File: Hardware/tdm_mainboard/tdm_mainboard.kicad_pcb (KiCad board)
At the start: 2 copper layers, 60 x 100 mm, 72 parts, among them IC1 W25Q128JVSIQ, J1 Headphone, J2 LineIn, J3 Conn_02x06_Top_Bottom, U1 AP7313, U2 PAM8302AASCR, U3 SGTL5000, U4 Teensy4, U5 TPS61090RSAR, U6 MOUNTINGHOLE2.5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

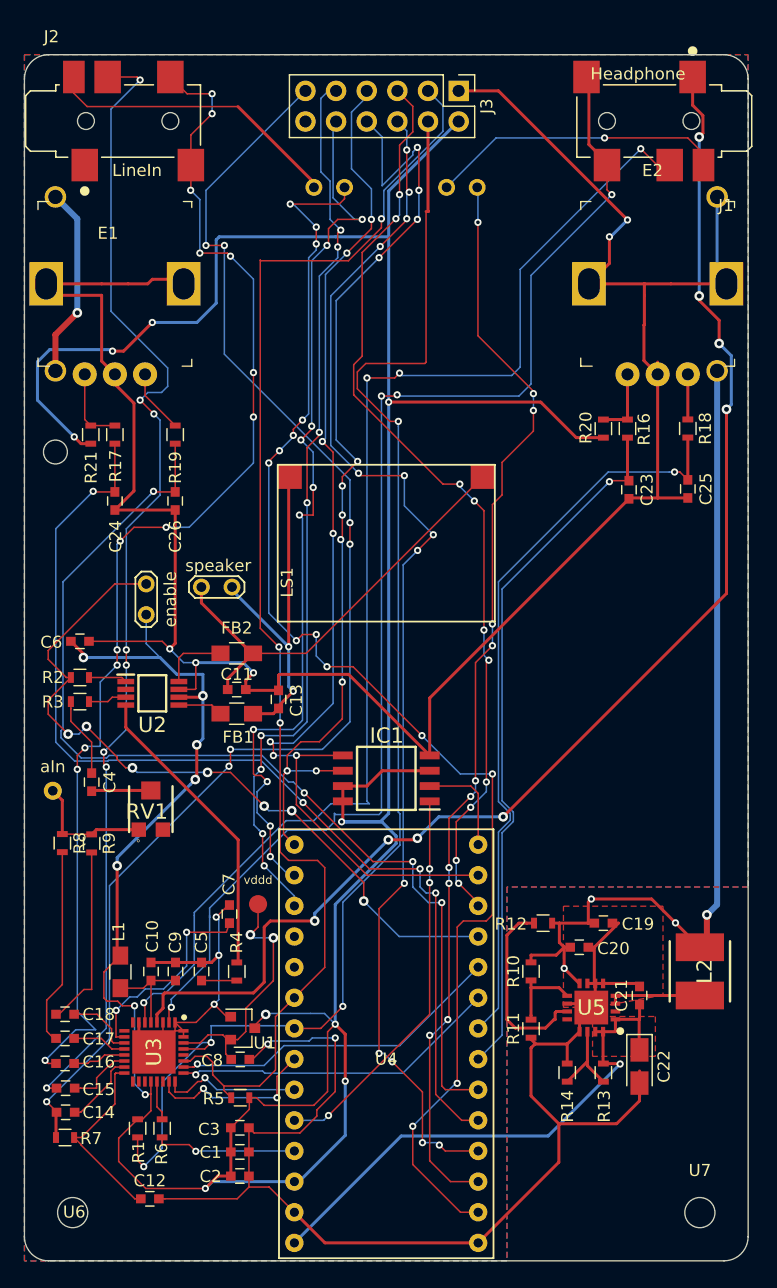
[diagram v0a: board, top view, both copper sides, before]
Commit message: some changes to the backboad
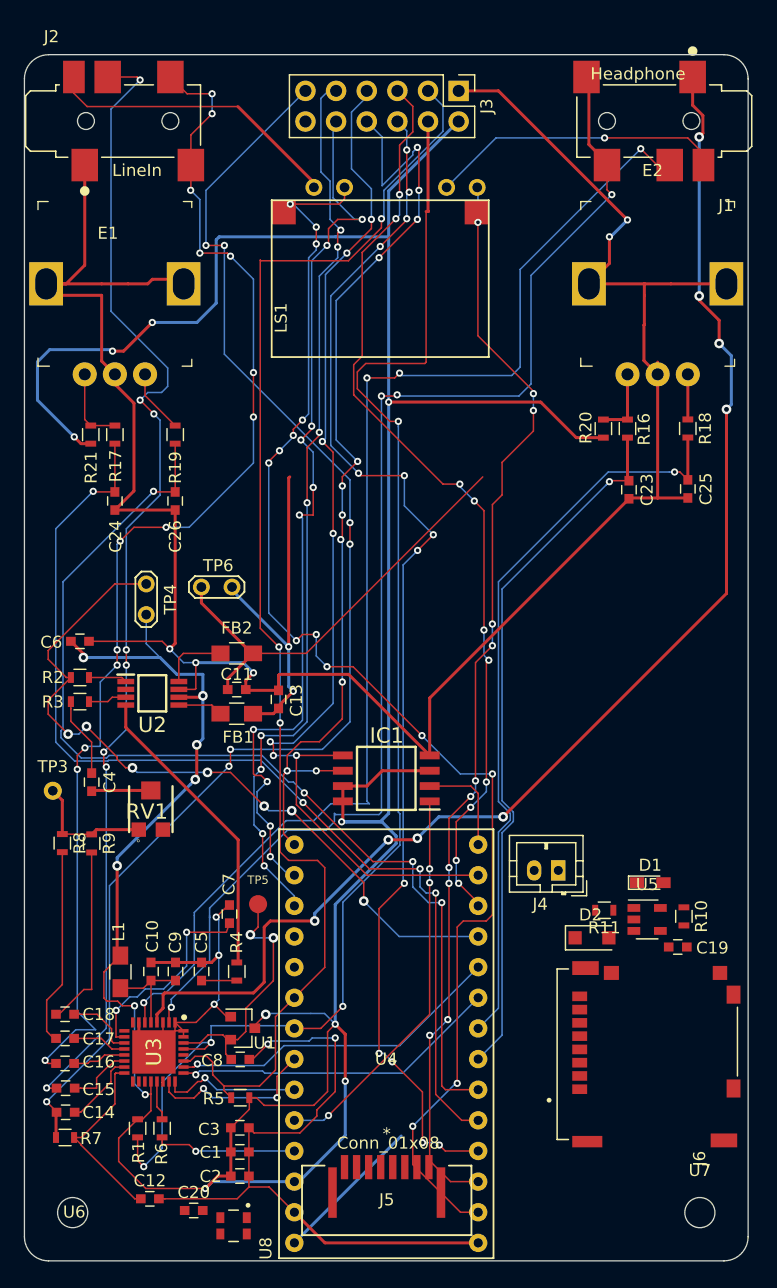
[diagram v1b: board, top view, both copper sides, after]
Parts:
- removed C21: 2.2uF, Capacitors_SMD:C_0603
- removed C22: 100uF electrolytic, Capacitors_Tantalum_SMD:CP_Tantalum_Case-A_EIA-3216-18_Reflow
- removed L2: VLC5045-6.8uH, SamacSys_Parts:INDPM5050X450N
- removed R12: 340K, Resistors_SMD:R_0603
- removed R13: 1.87M, Resistors_SMD:R_0603
- removed R14: 200K, Resistors_SMD:R_0603
- added D1: LED, LEDs:LED_0603_HandSoldering, F.Cu at (71.9, 88.6)
- added D2: mbr120, Diodes_SMD:D_SOD-123F, F.Cu at (67.1, 93.2)
- added J4: batteryConnection (jstph), Connectors_JST:JST_PH_B2B-PH-K_02x2.00mm_Straight, F.Cu at (64.3, 87.6)
- added J5: Conn_01x08, myLib:SFW8R-3STE1LF, F.Cu at (50.0, 109.5)
- added J6: 2908-05WB-MG, myLib:MOLEX_503182-1852_microsd, F.Cu at (72.4, 102.9)
- R10: value 1.87M -> 5k
- R11: value 340K -> 1k
- U5: value TPS61090RSAR -> MCP73831T-2ACI_OT; footprint SamacSys_Parts:QFN65P400X400X100-17N -> TO_SOT_Packages_SMD:SOT-23-5
- U8: value 1013 -> SPWmicrophone; footprint SamacSys_Parts:1013 -> myLib:MIC_SPW2430HR5H-B; moved to F.Cu
- moved U8 79.1 mm to (37.3, 117.1), turned to 270 degrees
- moved C20 38.7 mm to (34.0, 115.8)
- moved LS1 21.9 mm to (47.5, 36.1)
- moved R10 13.5 mm to (74.7, 91.4), turned to 270 degrees
- moved R11 11.5 mm to (68.1, 90.9), turned to 180 degrees
- moved U5 8.65 mm to (71.6, 91.7), turned to 0 degrees
- moved C19 6.48 mm to (74.2, 94.0)
- renumbered aIn to TP3, enable to TP4, vddd to TP5, speaker to TP6
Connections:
- C14 pad 2: MIC -> mic
- C20 pad 1: battery -> GND
- C20 pad 2: GND -> +3V3
- J3 pad 11: MIC -> (no net)
- R10 pad 2: battery -> GND
- R11 pad 1: GND -> Net-(R11-Pad1)
- R11 pad 2: Net-(R10-Pad1) -> Net-(D1-Pad1)
- R7 pad 1: MIC -> mic
- U3 pad 25: DIN -> DOUT
- U3 pad 26: DOUT -> DIN
- U4 pad Vin: 5.0V -> batteryPower
- U5 pad 1: 5.0V -> Net-(R11-Pad1)
- U5 pad 2: (no net) -> GND
- U5 pad 3: Net-(L2-PadP$2) -> battery
- U5 pad 4: Net-(L2-PadP$2) -> vbus
- U5 pad 5: GND -> Net-(R10-Pad1)
- U8 pad 1: Net-(U8-Pad1) -> GND
- U8 pad 2: Net-(U8-Pad1) -> +3V3
- U8 pad 3: GND -> mic
- U8 pad 4: battery -> (no net)
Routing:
- net battery: track 74.5 -> 0.00 mm, vias 4 -> 0
- net GND: track 340.0 -> 290.9 mm
- net 5.0V: track 45.5 -> 0.00 mm, vias 1 -> 0
- net Net-(U8-Pad1): track 15.9 -> 0.00 mm, vias 1 -> 0
- net /ENABLE: track 15.9 -> 0.00 mm
- net batteryPower: track 0.00 -> 12.5 mm
- net Net-(L2-PadP$2): track 7.66 -> 0.00 mm
- net Net-(R13-Pad1): track 7.06 -> 0.00 mm
- net Net-(R10-Pad1): track 6.53 -> 0.00 mm
- removed copper zone on F.Cu, net 5.0V
- removed copper zone on B.Cu, net GND
- removed copper zone on F.Cu, net GND
